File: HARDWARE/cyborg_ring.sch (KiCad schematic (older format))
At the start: 35 parts, among them SW1 SW_SPDT, U1 ATtiny85_QFN20_1-5, U2 ATtiny85_QFN20_11-15

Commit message: localized schematic symbols. changed name. minor formatting changes.
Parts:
- removed SW1: SW_SPDT, KiCad_Footprints:ZF_SW_PCM12SMTR, symbol SW_SPDT
- added SW1: SW_PUSH, KiCad_Footprints:ZF_SW_B3U, symbol SW_PUSH
- NA1, NA2: value RST_PULLUP -> SW_JMP
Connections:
- wire segments 67 -> 69
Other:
- moved on the sheet: TP3, TP7
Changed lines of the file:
@@
 LIBS:contrib
 LIBS:valves
-LIBS:NeuroTinker_schematic_symbols
-LIBS:blink-ring-cache
+LIBS:sw_push
+LIBS:passive_cordwood_x2
+LIBS:passive_cordwood
+LIBS:led-res_cordwood
+LIBS:attiny85_qfn20_11-15
+LIBS:attiny85_qfn20_1-5
 EELAYER 25 0
 EELAYER END
-$Descr A3 16535 11693
+$Descr USLedger 17000 11000
 encoding utf-8
 Sheet 1 1
 Title "blink-ring"
-Date "2017-12-26"
-Rev "A"
+Date "2018-05-17"
+Rev "C"
 Comp ""
-Comment1 "MIT license"
+Comment1 "License: CC-BY-SA 4.0"
 Comment2 "(c) copyright 2017 zach fredin"
 Comment3 ""
@@
 	-1   0    0    -1
 $EndComp
-Wire Wire Line
-	5500 4050 4950 4050
-Wire Wire Line
-	5150 3850 5150 4250
-Wire Wire Line
-	5150 4550 5150 5300
-Wire Wire Line
-	5500 4750 4950 4750
 $Comp
 L VCC #PWR03
@@
 	0    1    1    0
 $EndComp
-Wire Wire Line
-	5400 2650 5200 2650
 $Comp
 L TEST TP3
 U 1 1 5A42DC11
-P 5600 2950
-F 0 "TP3" H 5600 3250 50  0000 C BNN
-F 1 "MISO" H 5600 3200 50  0000 C CNN
-F 2 "KiCad_Footprints:ZF_CONN_1-2_pad" H 5600 2950 50  0001 C CNN
-F 3 "" H 5600 2950 50  0001 C CNN
-	1    5600 2950
+P 6300 2950
+F 0 "TP3" H 6300 3250 50  0000 C BNN
+F 1 "MISO" H 6300 3200 50  0000 C CNN
+F 2 "KiCad_Footprints:ZF_CONN_1-2_pad" H 6300 2950 50  0001 C CNN
+F 3 "" H 6300 2950 50  0001 C CNN
+	1    6300 2950
 	0    1    1    0
 $EndComp
@@
 	0    1    1    0
 $EndComp
-Wire Wire Line
-	5400 3100 5200 3100
-Wire Wire Line
-	5200 2950 5600 2950
 $Comp
 L TEST TP5
@@
 	-1   0    0    -1
 $EndComp
-Wire Wire Line
-	5500 3850 5500 4050
-Connection ~ 5150 4050
 $Comp
 L TEST TP6
@@
 	-1   0    0    -1
 $EndComp
-Wire Wire Line
-	5500 4750 5500 4550
-Connection ~ 5150 4750
-Wire Wire Line
-	5600 1150 5600 2500
-Wire Wire Line
-	5600 2500 5200 2500
 $Comp
 L Passive_cordwood R2
@@
 	1    0    0    -1
 $EndComp
-Wire Wire Line
-	2800 4050 2600 4050
-Wire Wire Line
-	2600 4050 2600 4200
-$Comp
-L SW_SPDT SW1
-U 1 1 5A430BC6
-P 2600 4400
-F 0 "SW1" H 2600 4570 50  0000 C CNN
-F 1 "SW_SPDT" H 2600 4200 50  0000 C CNN
-F 2 "KiCad_Footprints:ZF_SW_PCM12SMTR" H 2600 4400 50  0001 C CNN
-F 3 "" H 2600 4400 50  0001 C CNN
-	1    2600 4400
-	0    1    1    0
-$EndComp
-Wire Wire Line
-	2800 4750 2700 4750
-Wire Wire Line
-	2700 4750 2700 4600
-$Comp
-L Passive_cordwood_x2 NA2
-U 1 1 5A43122D
-P 4900 1700
-F 0 "NA2" H 4900 1575 60  0000 C CNN
-F 1 "RST_PULLUP" H 4900 1825 60  0000 C CNN
-F 2 "KiCad_Footprints:ZF_SMD_0805_CORD" H 4900 1700 60  0001 C CNN
-F 3 "" H 4900 1700 60  0001 C CNN
-	1    4900 1700
-	-1   0    0    1
-$EndComp
-Wire Wire Line
-	5200 1700 5600 1700
-Connection ~ 5600 1700
 $Comp
 L C C1
@@
 	1    0    0    -1
 $EndComp
-$Comp
-L Passive_cordwood_x2 NA1
-U 1 1 5A432159
-P 2900 1700
-F 0 "NA1" H 2900 1575 60  0000 C CNN
-F 1 "RST_PULLUP" H 2900 1825 60  0000 C CNN
-F 2 "KiCad_Footprints:ZF_SMD_0805_CORD" H 2900 1700 60  0001 C CNN
-F 3 "" H 2900 1700 60  0001 C CNN
-	1    2900 1700
-	1    0    0    -1
-$EndComp
-Wire Wire Line
-	2600 1700 2300 1700
-Wire Wire Line
-	2300 1700 2300 2500
-Wire Wire Line
-	2000 2500 2550 2500
 $Comp
 L TEST TP1
@@
 	0    -1   -1   0
 $EndComp
-Connection ~ 2300 2500
 Text Label 2300 2650 2    60   ~ 0
 LED_BOTTOM_0
-Wire Wire Line
-	2300 2650 2550 2650
 Text Label 2300 3100 2    60   ~ 0
 LED_BOTTOM_1
-Wire Wire Line
-	2300 3100 2550 3100
 Text Label 5550 3300 0    60   ~ 0
 LED_TOP_1
-Wire Wire Line
-	5550 3300 5300 3300
-Wire Wire Line
-	5300 3300 5300 3100
-Connection ~ 5300 3100
 Text Label 5550 2800 0    60   ~ 0
 LED_TOP_0
-Wire Wire Line
-	5550 2800 5300 2800
-Wire Wire Line
-	5300 2800 5300 2650
-Connection ~ 5300 2650
-Wire Wire Line
-	4950 5100 5150 5100
-Connection ~ 5150 5100
 $Comp
 L TEST TP7
 U 1 1 5A433B99
-P 2600 5100
-F 0 "TP7" H 2600 5400 50  0000 C BNN
-F 1 "GND" H 2600 5350 50  0000 C CNN
-F 2 "KiCad_Footprints:ZF_CONN_1-2_pad" H 2600 5100 50  0001 C CNN
-F 3 "" H 2600 5100 50  0001 C CNN
-	1    2600 5100
-	0    -1   1    0
-$EndComp
-Wire Wire Line
-	2600 5100 2800 5100
+P 2100 4900
+F 0 "TP7" H 2100 5200 50  0000 C BNN
+F 1 "GND" H 2100 5150 50  0000 C CNN
+F 2 "KiCad_Footprints:ZF_CONN_1-2_pad" H 2100 4900 50  0001 C CNN
+F 3 "" H 2100 4900 50  0001 C CNN
+	1    2100 4900
+	-1   0    0    -1
+$EndComp
 $Comp
 L Passive_cordwood_x2 NA3
@@
 	-1   0    0    1
 $EndComp
-Wire Notes Line
-	3800 11200 3850 11200
 $Comp
 L LED-RES_cordwood D1
@@
 	1    0    0    -1
 $EndComp
-Wire Wire Line
-	3200 5900 3000 5900
-Wire Wire Line
-	3000 5900 3000 6400
-Wire Wire Line
-	4500 6400 4500 5900
-Wire Wire Line
-	4500 5900 4300 5900
-Wire Wire Line
-	4350 6400 4500 6400
-Wire Wire Line
-	3000 6400 3250 6400
 $Comp
 L Passive_cordwood R7
@@
 	1    0    0    -1
 $EndComp
-Wire Wire Line
-	3200 6900 3000 6900
-Wire Wire Line
-	3000 6900 3000 7400
-Wire Wire Line
-	4500 7400 4500 6900
-Wire Wire Line
-	4500 6900 4300 6900
-Wire Wire Line
-	4350 7400 4500 7400
-Wire Wire Line
-	3000 7400 3250 7400
-Wire Wire Line
-	3000 7150 2800 7150
-Wire Wire Line
-	2800 7150 2800 6150
-Wire Wire Line
-	2800 6150 3000 6150
-Connection ~ 3000 6150
-Connection ~ 3000 7150
 $Comp
 L Passive_cordwood R9
@@
 	1    0    0    -1
 $EndComp
-Wire Wire Line
-	3200 7900 3000 7900
-Wire Wire Line
-	3000 7900 3000 8400
-Wire Wire Line
-	4500 8400 4500 7900
-Wire Wire Line
-	4500 7900 4300 7900
-Wire Wire Line
-	4350 8400 4500 8400
-Wire Wire Line
-	3000 8400 3250 8400
-Wire Wire Line
-	4500 8150 4700 8150
-Wire Wire Line
-	4700 8150 4700 7150
-Wire Wire Line
-	4700 7150 4500 7150
-Connection ~ 4500 7150
-Connection ~ 4500 8150
 $Comp
 L Passive_cordwood R11
@@
 	1    0    0    -1
 $EndComp
+Text Label 2600 6700 2    60   ~ 0
+LED_BOTTOM_0
+Text Label 2600 8700 2    60   ~ 0
+LED_BOTTOM_1
+Text Label 5100 6700 0    60   ~ 0
+LED_TOP_0
+Text Label 5100 7650 0    60   ~ 0
+LED_TOP_1
+Wire Wire Line
+	5500 4050 4950 4050
+Wire Wire Line
+	5150 3850 5150 4250
+Wire Wire Line
+	5150 4550 5150 5300
+Wire Wire Line
+	5500 4750 4950 4750
+Wire Wire Line
+	5400 2650 5200 2650
+Wire Wire Line
+	5400 3100 5200 3100
+Wire Wire Line
+	5200 2950 6300 2950
+Wire Wire Line
+	5500 3850 5500 4050
+Connection ~ 5150 4050
+Wire Wire Line
+	5500 4750 5500 4550
+Connection ~ 5150 4750
+Wire Wire Line
+	5600 1150 5600 2500
+Wire Wire Line
+	5600 2500 5200 2500
+Wire Wire Line
+	2700 4750 2800 4750
+Wire Wire Line
+	2700 4050 2700 4750
+Wire Wire Line
+	2000 2500 2550 2500
+Wire Wire Line
+	2300 2650 2550 2650
+Wire Wire Line
+	2300 3100 2550 3100
+Wire Wire Line
+	5550 3300 5300 3300
+Wire Wire Line
+	5300 3300 5300 3100
+Connection ~ 5300 3100
+Wire Wire Line
+	5550 2800 5300 2800
+Wire Wire Line
+	5300 2800 5300 2650
+Connection ~ 5300 2650
+Wire Wire Line
+	4950 5100 5150 5100
+Connection ~ 5150 5100
+Wire Wire Line
+	1400 5100 2800 5100
+Wire Notes Line
+	3800 11200 3850 11200
+Wire Wire Line
+	3200 5900 3000 5900
+Wire Wire Line
+	3000 5900 3000 6400
+Wire Wire Line
+	4500 6400 4500 5900
+Wire Wire Line
+	4500 5900 4300 5900
+Wire Wire Line
+	4350 6400 4500 6400
+Wire Wire Line
+	3000 6400 3250 6400
+Wire Wire Line
+	3200 6900 3000 6900
+Wire Wire Line
+	3000 6900 3000 7400
+Wire Wire Line
+	4500 7400 4500 6900
+Wire Wire Line
+	4500 6900 4300 6900
+Wire Wire Line
+	4350 7400 4500 7400
+Wire Wire Line
+	3000 7400 3250 7400
+Wire Wire Line
+	3000 7150 2800 7150
+Wire Wire Line
+	2800 7150 2800 6150
+Wire Wire Line
+	2800 6150 3000 6150
+Connection ~ 3000 6150
+Connection ~ 3000 7150
+Wire Wire Line
+	3200 7900 3000 7900
+Wire Wire Line
+	3000 7900 3000 8400
+Wire Wire Line
+	4500 8400 4500 7900
+Wire Wire Line
+	4500 7900 4300 7900
+Wire Wire Line
+	4350 8400 4500 8400
+Wire Wire Line
+	3000 8400 3250 8400
+Wire Wire Line
+	4500 8150 4700 8150
+Wire Wire Line
+	4700 8150 4700 7150
+Wire Wire Line
+	4700 7150 4500 7150
+Connection ~ 4500 7150
+Connection ~ 4500 8150
 Wire Wire Line
 	3200 8900 3000 8900
@@
 Connection ~ 4500 6150
 Connection ~ 4500 9150
-Text Label 2600 6700 2    60   ~ 0
-LED_BOTTOM_0
 Wire Wire Line
 	2600 6700 2800 6700
 Connection ~ 2800 6700
-Text Label 2600 8700 2    60   ~ 0
-LED_BOTTOM_1
 Wire Wire Line
 	2600 8700 2800 8700
 Connection ~ 2800 8700
-Text Label 5100 6700 0    60   ~ 0
-LED_TOP_0
 Wire Wire Line
 	5100 6700 4900 6700
 Connection ~ 4900 6700
-Text Label 5100 7650 0    60   ~ 0
-LED_TOP_1
 Wire Wire Line
 	5100 7650 4700 7650
@@
 Wire Notes Line
 	3800 10700 3800 500
+Wire Wire Line
+	2800 4050 2700 4050
+$Comp
+L Passive_cordwood_x2 NA2
+U 1 1 5A43122D
+P 4900 1700
+F 0 "NA2" H 4900 1575 60  0000 C CNN
+F 1 "SW_JMP" H 4900 1825 60  0000 C CNN
+F 2 "KiCad_Footprints:ZF_SMD_0805_CORD" H 4900 1700 60  0001 C CNN
+F 3 "" H 4900 1700 60  0001 C CNN
+	1    4900 1700
+	-1   0    0    1
+$EndComp
+Wire Wire Line
+	2600 1700 2300 1700
+$Comp
+L Passive_cordwood_x2 NA1
+U 1 1 5A432159
+P 2900 1700
+F 0 "NA1" H 2900 1575 60  0000 C CNN
+F 1 "SW_JMP" H 2900 1825 60  0000 C CNN
+F 2 "KiCad_Footprints:ZF_SMD_0805_CORD" H 2900 1700 60  0001 C CNN
+F 3 "" H 2900 1700 60  0001 C CNN
+	1    2900 1700
+	1    0    0    -1
+$EndComp
+Wire Wire Line
+	5200 1700 6150 1700
+Wire Wire Line
+	6150 1700 6150 2950
+Connection ~ 6150 2950
+$Comp
+L SW_PUSH SW1
+U 1 1 5A4A7E66
+P 2000 1700
+F 0 "SW1" H 2150 1810 50  0000 C CNN
+F 1 "SW_PUSH" H 2000 1620 50  0000 C CNN
+F 2 "KiCad_Footprints:ZF_SW_B3U" H 2000 1700 50  0001 C CNN
+F 3 "" H 2000 1700 50  0000 C CNN
+F 4 "No" H 2000 1700 60  0001 C CNN "Subs Allowed"
+F 5 "Yes" H 2000 1700 60  0001 C CNN "RoHS"
+	1    2000 1700
+	1    0    0    -1
+$EndComp
+Wire Wire Line
+	1400 1700 1400 5100
+Wire Wire Line
+	1400 1700 1700 1700
+Wire Wire Line
+	2100 4900 2100 5100
+Connection ~ 2100 5100
 $EndSCHEMATC

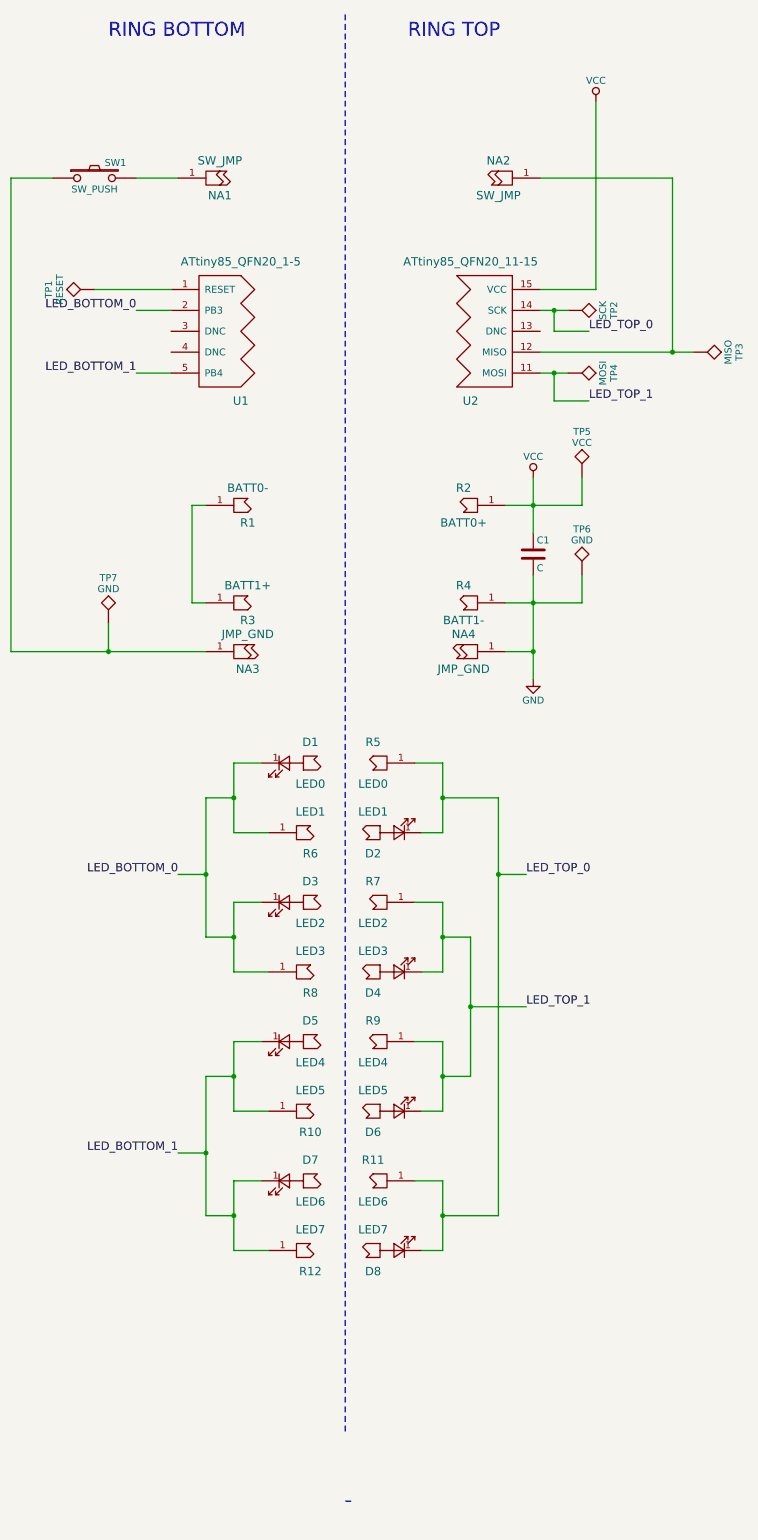
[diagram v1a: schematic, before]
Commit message: added 10M+10M R0805+R0805 reinforcement resistors to BOM and schematic. updated component references on schematic, BOM, and layout to start with 'BOT_' or 'TOP_' for cordwood-style installations. minor schematic readability improvements.
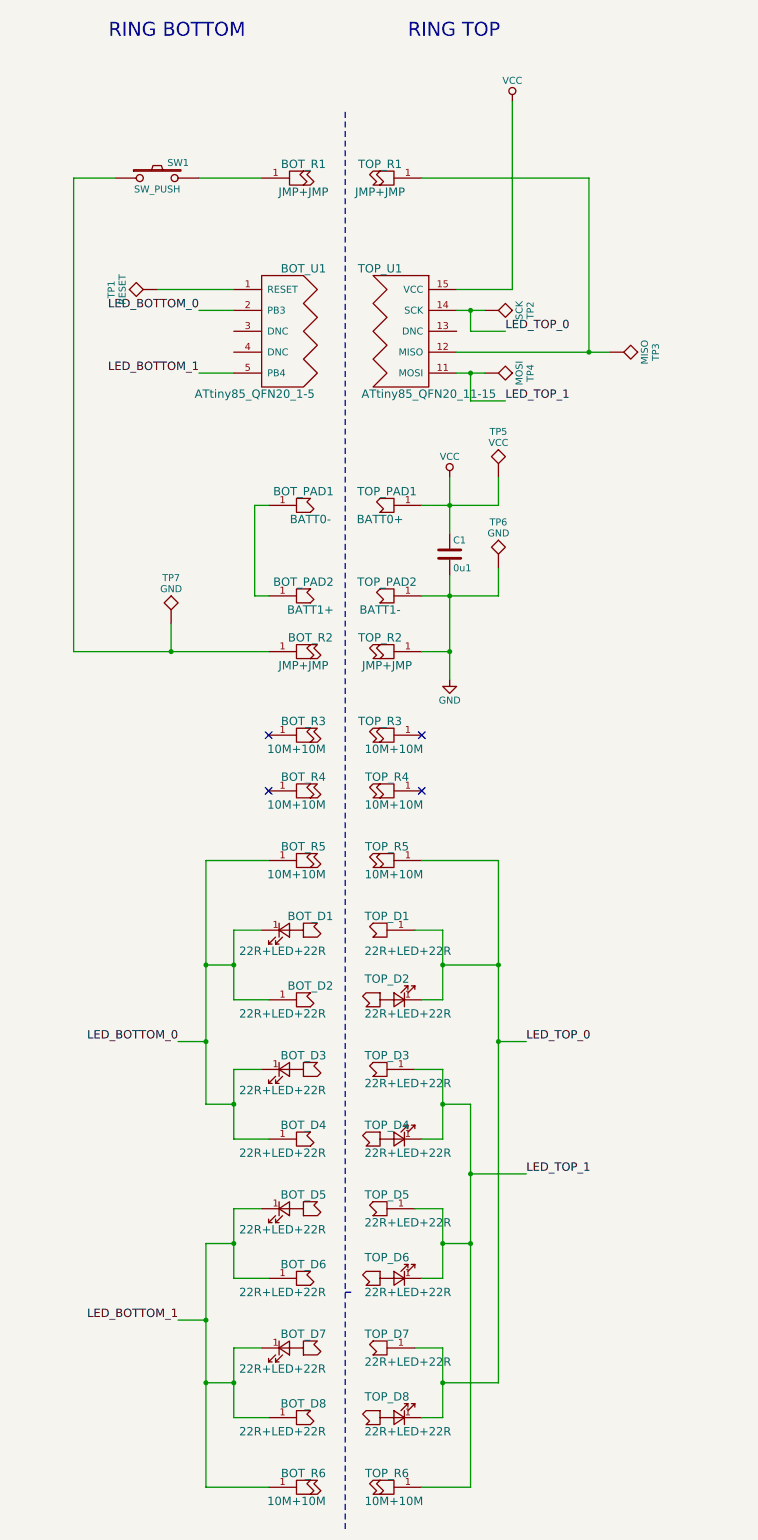
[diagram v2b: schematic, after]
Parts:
- added BOT_R3, BOT_R4, BOT_R5, BOT_R6, TOP_R3, TOP_R4, TOP_R5, TOP_R6: 10M+10M, KiCad_Footprints:ZF_SMD_0805_CORD, symbol Passive_cordwood_x2
- BOT_D1: renamed from D1; value LED0 -> 22R+LED+22R; Link (none) -> https://www.digikey.com/product-detail/en/rohm-semiconducto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; Package (none) -> R0508+LED0603+R0508; RoHS (none) -> Yes; Subs Allowed (none) -> No
- BOT_D2: renamed from R6; value LED1 -> 22R+LED+22R; Link (none) -> https://www.digikey.com/product-detail/en/rohm-semiconducto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; Package (none) -> R0508+LED0603+R0508; RoHS (none) -> Yes; Subs Allowed (none) -> No
- BOT_D3: renamed from D3; value LED2 -> 22R+LED+22R; Link (none) -> https://www.digikey.com/product-detail/en/rohm-semiconducto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; Package (none) -> R0508+LED0603+R0508; RoHS (none) -> Yes; Subs Allowed (none) -> No
- BOT_D4: renamed from R8; value LED3 -> 22R+LED+22R; Link (none) -> https://www.digikey.com/product-detail/en/rohm-semiconducto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; Package (none) -> R0508+LED0603+R0508; RoHS (none) -> Yes; Subs Allowed (none) -> No
- BOT_D5: renamed from D5; value LED4 -> 22R+LED+22R; Link (none) -> https://www.digikey.com/product-detail/en/rohm-semiconducto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; Package (none) -> R0508+LED0603+R0508; RoHS (none) -> Yes; Subs Allowed (none) -> No
- BOT_D6: renamed from R10; value LED5 -> 22R+LED+22R; Link (none) -> https://www.digikey.com/product-detail/en/rohm-semiconducto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; Package (none) -> R0508+LED0603+R0508; RoHS (none) -> Yes; Subs Allowed (none) -> No
- BOT_D7: renamed from D7; value LED6 -> 22R+LED+22R; Link (none) -> https://www.digikey.com/product-detail/en/rohm-semiconducto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; Package (none) -> R0508+LED0603+R0508; RoHS (none) -> Yes; Subs Allowed (none) -> No
- BOT_D8: renamed from R12; value LED7 -> 22R+LED+22R; Link (none) -> https://www.digikey.com/product-detail/en/rohm-semiconducto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; Package (none) -> R0508+LED0603+R0508; RoHS (none) -> Yes; Subs Allowed (none) -> No
- BOT_PAD1: renamed from R1; Link (none) -> https://www.digikey.com/product-detail/en/te-connectivity-a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; Mfr (none) -> TE Connectivity; Mfr Part # (none) -> 1447360-8; Package (none) -> SMT; RoHS (none) -> Yes; Subs Allowed (none) -> No
- BOT_PAD2: renamed from R3; Package (none) -> ENIG pad; RoHS (none) -> Yes; Subs Allowed (none) -> No
- BOT_R1: renamed from NA1; value SW_JMP -> JMP+JMP; Package (none) -> R0805+R0805; RoHS (none) -> Yes; Subs Allowed (none) -> Yes
- BOT_R2: renamed from NA3; value JMP_GND -> JMP+JMP; Package (none) -> R0805+R0805; RoHS (none) -> Yes; Subs Allowed (none) -> Yes
- BOT_U1: renamed from U1; Link (none) -> https://www.digikey.com/product-detail/en/microchip-technol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; Mfr (none) -> Atmel/Microchip; Mfr Part # (none) -> ATTINY85-20MUR; Package (none) -> QFN20-0.5; RoHS (none) -> Yes; Subs Allowed (none) -> No
- C1: value C -> 0u1; Package (none) -> C0402; RoHS (none) -> Yes; Subs Allowed (none) -> Yes
- SW1: Link (none) -> https://www.digikey.com/product-detail/en/omron-electronics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; Mfr (none) -> Omron Electronics; Mfr Part # (none) -> B3U-3000P; Package (none) -> SMT
- TOP_D1: renamed from R5; value LED0 -> 22R+LED+22R; Link (none) -> https://www.digikey.com/product-detail/en/rohm-semiconducto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; Package (none) -> R0508+LED0603+R0508; RoHS (none) -> Yes; Subs Allowed (none) -> No
- TOP_D2: renamed from D2; value LED1 -> 22R+LED+22R; Link (none) -> https://www.digikey.com/product-detail/en/rohm-semiconducto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; Package (none) -> R0508+LED0603+R0508; RoHS (none) -> Yes; Subs Allowed (none) -> No
- TOP_D3: renamed from R7; value LED2 -> 22R+LED+22R; Link (none) -> https://www.digikey.com/product-detail/en/rohm-semiconducto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; Package (none) -> R0508+LED0603+R0508; RoHS (none) -> Yes; Subs Allowed (none) -> No
- TOP_D4: renamed from D4; value LED3 -> 22R+LED+22R; Link (none) -> https://www.digikey.com/product-detail/en/rohm-semiconducto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; Package (none) -> R0508+LED0603+R0508; RoHS (none) -> Yes; Subs Allowed (none) -> No
- TOP_D5: renamed from R9; value LED4 -> 22R+LED+22R; Link (none) -> https://www.digikey.com/product-detail/en/rohm-semiconducto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; Package (none) -> R0508+LED0603+R0508; RoHS (none) -> Yes; Subs Allowed (none) -> No
- TOP_D6: renamed from D6; value LED5 -> 22R+LED+22R; Link (none) -> https://www.digikey.com/product-detail/en/rohm-semiconducto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; Package (none) -> R0508+LED0603+R0508; RoHS (none) -> Yes; Subs Allowed (none) -> No
- TOP_D7: renamed from R11; value LED6 -> 22R+LED+22R; Link (none) -> https://www.digikey.com/product-detail/en/rohm-semiconducto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; Package (none) -> R0508+LED0603+R0508; RoHS (none) -> Yes; Subs Allowed (none) -> No
- TOP_D8: renamed from D8; value LED7 -> 22R+LED+22R; Link (none) -> https://www.digikey.com/product-detail/en/rohm-semiconducto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; Package (none) -> R0508+LED0603+R0508; RoHS (none) -> Yes; Subs Allowed (none) -> No
- TOP_PAD1: renamed from R2; Package (none) -> ENIG pad; RoHS (none) -> Yes; Subs Allowed (none) -> No
- TOP_PAD2: renamed from R4; Link (none) -> https://www.digikey.com/product-detail/en/te-connectivity-a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; Mfr (none) -> TE Connectivity; Mfr Part # (none) -> 1447360-8; Package (none) -> SMT; RoHS (none) -> Yes; Subs Allowed (none) -> No
- TOP_R1: renamed from NA2; value SW_JMP -> JMP+JMP; Package (none) -> R0805+R0805; RoHS (none) -> Yes; Subs Allowed (none) -> Yes
- TOP_R2: renamed from NA4; value JMP_GND -> JMP+JMP; Package (none) -> R0805+R0805; RoHS (none) -> Yes; Subs Allowed (none) -> Yes
- TOP_U1: renamed from U2; Link (none) -> https://www.digikey.com/product-detail/en/microchip-technol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; Mfr (none) -> Atmel/Microchip; Mfr Part # (none) -> ATTINY85-20MUR; Package (none) -> QFN20-0.5; RoHS (none) -> Yes; Subs Allowed (none) -> No
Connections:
- net LED_BOTTOM_0: now also BOT_R5.1
- net LED_BOTTOM_1: now also BOT_R6.1
- net LED_TOP_0: now also TOP_R5.1
- net LED_TOP_1: now also TOP_R6.1
- no-connect marks 0 -> 4
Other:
- moved on the sheet: BOT_D1, BOT_D2, BOT_D3, BOT_D4, BOT_D5, BOT_D6, BOT_D7, BOT_D8, BOT_PAD1, BOT_PAD2, BOT_R1, BOT_R2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
